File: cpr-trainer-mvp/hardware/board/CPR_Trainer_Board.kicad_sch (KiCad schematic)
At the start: 8 parts, among them J1 ADXL355, J4 ESP32, SW1 SW

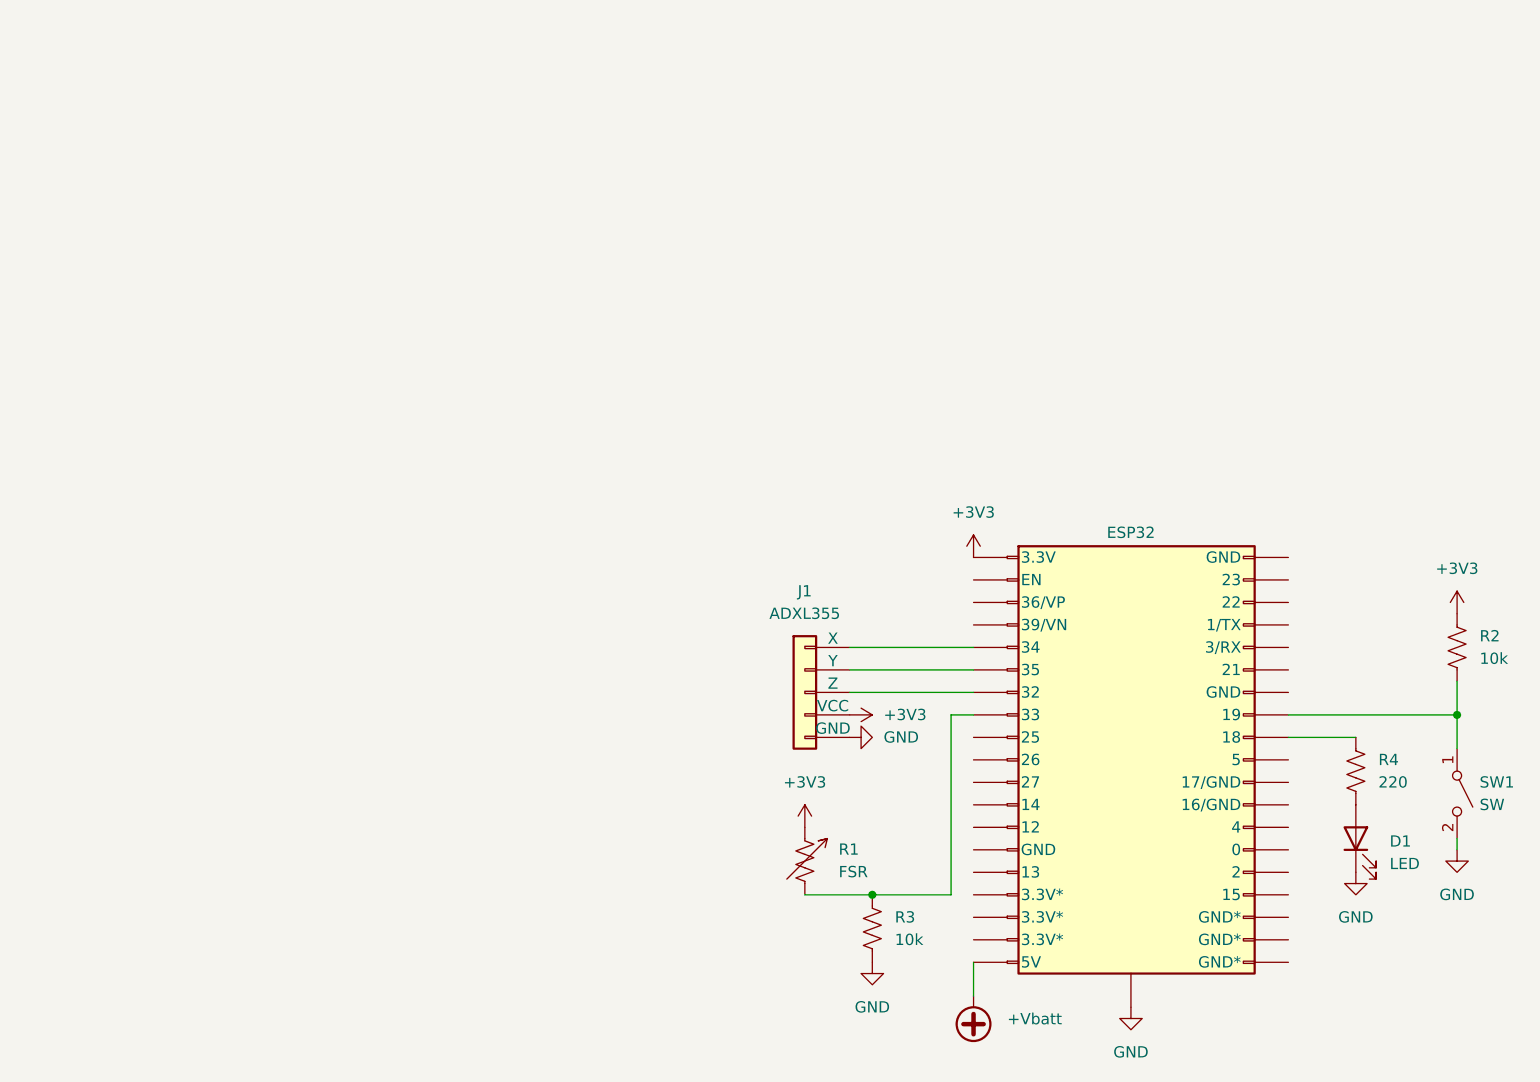
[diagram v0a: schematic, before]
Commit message: Updated README.md format, Refined circuit KiCad
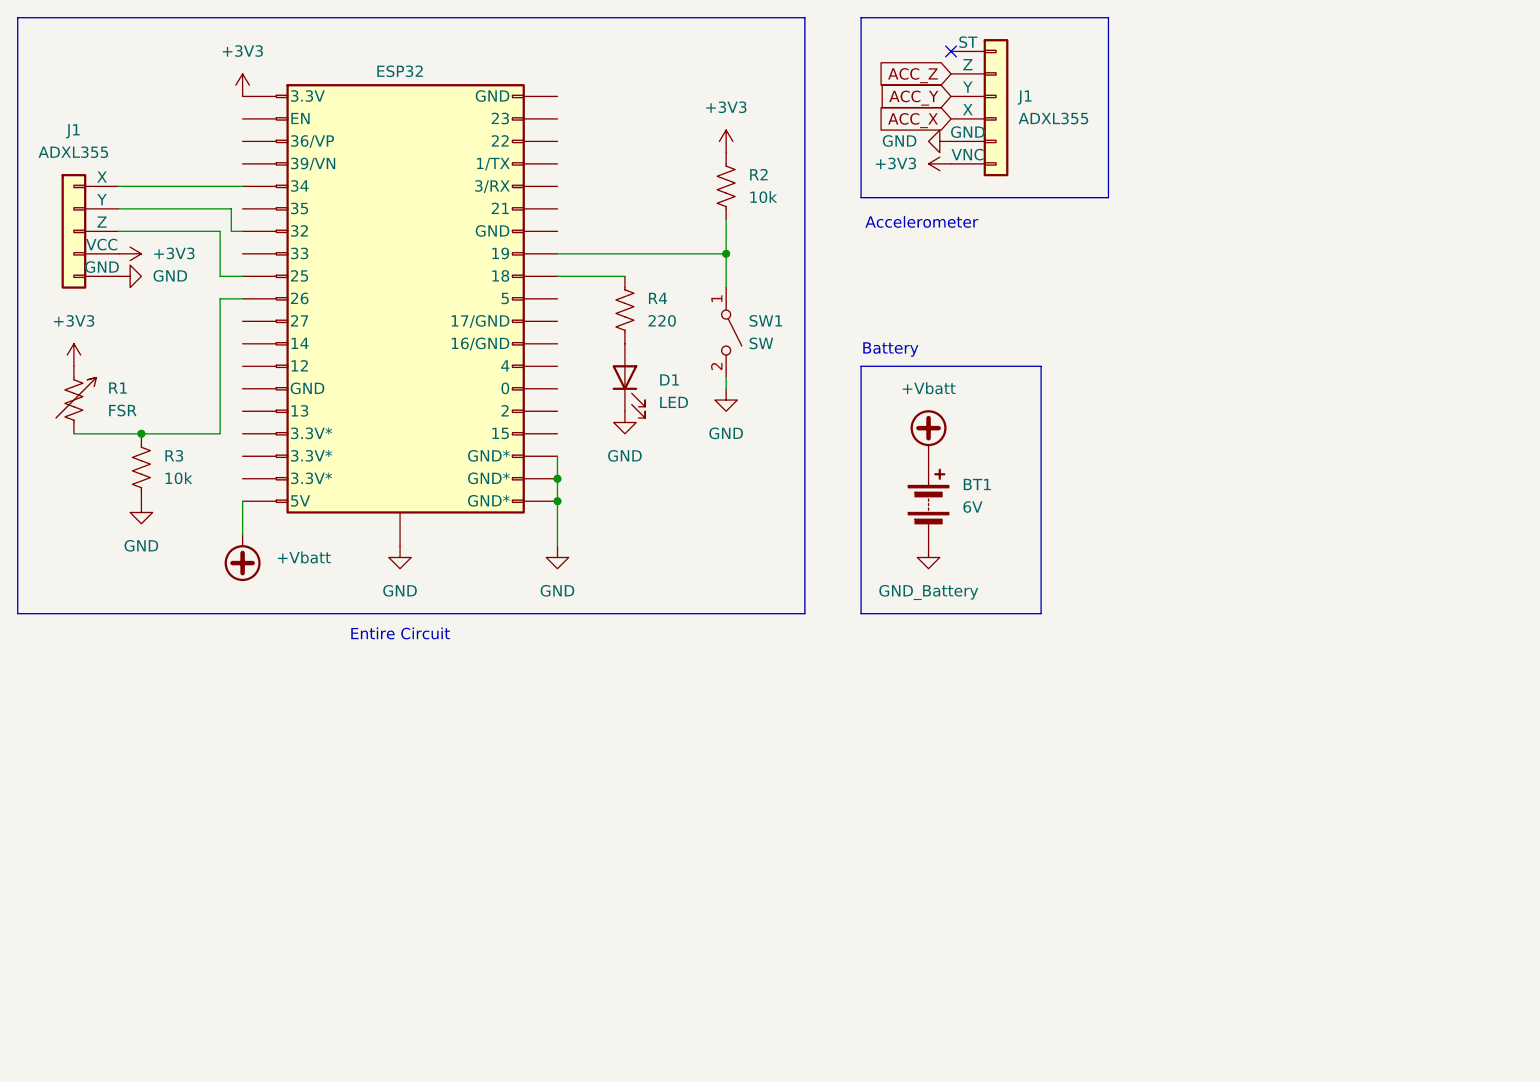
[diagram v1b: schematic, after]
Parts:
- added BT1: 6V, symbol Device:Battery
- added J1: ADXL355, symbol Connector_Generic:Conn_01x06
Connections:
- net +3V3: now also J1.6 (VNC)
- net +Vbatt: now also BT1.1 (+)
- net GND: now also J4.20 (GND*), J4.21 (GND*), J4.22 (GND*), J1.5 (GND)
- net at R1.2, R3.1: now also J4.10 (26); no longer J4.8 (33)
- net at J1.2 (Y): now also J4.7 (32); no longer J4.6 (35)
- net at J1.3 (Z): now also J4.9 (25); no longer J4.7 (32)
- new net ACC_X: J1.4 (X)
- new net ACC_Y: J1.3 (Y)
- new net ACC_Z: J1.2 (Z)
- new net GND_Battery: BT1.2 (-)
- no-connect marks 0 -> 1
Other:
- note added: "Accelerometer"
- note added: "Battery"
- note added: "Entire Circuit"
- moved on the sheet: D1, J1, R1, R2, R3, R4, SW1
